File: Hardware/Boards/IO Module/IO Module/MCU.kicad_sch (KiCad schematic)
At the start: 21 parts, among them SW1 RST, U14 W25Q16JVUXIQ TR, U15 RP2040, Y3 12Mhz

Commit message: Completed IO Module PCB Layout
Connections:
- net MBUS_D0: now also U15.18 (GPIO15); no longer U15.11 (GPIO8)
- net MBUS_D1: now also U15.17 (GPIO14); no longer U15.12 (GPIO9)
- net MBUS_D10: now also U15.31 (GPIO20); no longer U15.29 (GPIO18)
- net MBUS_D11: now also U15.32 (GPIO21); no longer U15.30 (GPIO19)
- net MBUS_D12: now also U15.34 (GPIO22); no longer U15.31 (GPIO20)
- net MBUS_D13: now also U15.35 (GPIO23); no longer U15.32 (GPIO21)
- net MBUS_D14: now also U15.28 (GPIO17); no longer U15.34 (GPIO22)
- net MBUS_D15: now also U15.27 (GPIO16); no longer U15.35 (GPIO23)
- net MBUS_D2: now also U15.16 (GPIO13); no longer U15.13 (GPIO10)
- net MBUS_D3: now also U15.15 (GPIO12); no longer U15.14 (GPIO11)
- net MBUS_D4: now also U15.11 (GPIO8); no longer U15.15 (GPIO12)
- net MBUS_D5: now also U15.12 (GPIO9); no longer U15.16 (GPIO13)
- net MBUS_D6: now also U15.13 (GPIO10); no longer U15.17 (GPIO14)
- net MBUS_D7: now also U15.14 (GPIO11); no longer U15.18 (GPIO15)
- net MBUS_D8: now also U15.29 (GPIO18); no longer U15.27 (GPIO16)
- net MBUS_D9: now also U15.30 (GPIO19); no longer U15.28 (GPIO17)
- net USBPD_FLT_IN: now also U15.38 (GPIO26_ADC0); no longer U15.36 (GPIO24)
- net USBPD_SINK_EN: now also U15.36 (GPIO24); no longer U15.38 (GPIO26_ADC0)
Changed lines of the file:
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@@
+		)
+	)
+	(label "MBUS_D15"
+		(at 227.33 154.94 0)
+		(fields_autoplaced yes)
+		(effects
+			(font
+				(size 1.27 1.27)
+			)
+			(justify left bottom)
+		)
+	)
+	(label "MBUS_D6"
+		(at 227.33 139.7 0)
+		(fields_autoplaced yes)
+		(effects
+			(font
+				(size 1.27 1.27)
+			)
+			(justify left bottom)
 		)
 	)
@@
 		)
 	)
-	(label "MBUS_D0"
-		(at 227.33 134.62 0)
-		(fields_autoplaced yes)
-		(effects
-			(font
-				(size 1.27 1.27)
-			)
-			(justify left bottom)
-		)
-	)
 	(label "USBPD_PLG_EVNT"
 		(at 224.79 116.84 0)
@@
 		)
 	)
-	(label "MBUS_D13"
-		(at 227.33 167.64 0)
-		(fields_autoplaced yes)
-		(effects
-			(font
-				(size 1.27 1.27)
-			)
-			(justify left bottom)
-		)
-	)
-	(label "MBUS_D10"
-		(at 227.33 160.02 0)
-		(fields_autoplaced yes)
-		(effects
-			(font
-				(size 1.27 1.27)
-			)
-			(justify left bottom)
-		)
-	)
-	(label "MBUS_D15"
-		(at 227.33 172.72 0)
+	(label "MBUS_D7"
+		(at 227.33 142.24 0)
+		(fields_autoplaced yes)
+		(effects
+			(font
+				(size 1.27 1.27)
+			)
+			(justify left bottom)
+		)
+	)
+	(label "MBUS_D2"
+		(at 227.33 147.32 0)
 		(fields_autoplaced yes)
 		(effects
@@
 	)
 	(label "USBPD_FLT_IN"
-		(at 224.79 175.26 0)
-		(fields_autoplaced yes)
-		(effects
-			(font
-				(size 1.27 1.27)
-			)
-			(justify left bottom)
-		)
-	)
-	(label "MBUS_D14"
-		(at 227.33 170.18 0)
+		(at 224.79 182.88 0)
 		(fields_autoplaced yes)
 		(effects
@@
 		)
 	)
+	(label "MBUS_D12"
+		(at 227.33 170.18 0)
+		(fields_autoplaced yes)
+		(effects
+			(font
+				(size 1.27 1.27)
+			)
+			(justify left bottom)
+		)
+	)
 	(label "QSPI_D0"
 		(at 149.86 137.16 0)
@@
 		)
 	)
+	(label "MBUS_D3"
+		(at 227.33 144.78 0)
+		(fields_autoplaced yes)
+		(effects
+			(font
+				(size 1.27 1.27)
+			)
+			(justify left bottom)
+		)
+	)
 	(label "USBPD_CAP_MIS"
 		(at 224.79 187.96 0)
@@
 	)
 	(label "MBUS_D9"
-		(at 227.33 157.48 0)
-		(fields_autoplaced yes)
-		(effects
-			(font
-				(size 1.27 1.27)
-			)
-			(justify left bottom)
-		)
-	)
-	(label "MBUS_D7"
-		(at 227.33 152.4 0)
-		(fields_autoplaced yes)
-		(effects
-			(font
-				(size 1.27 1.27)
-			)
-			(justify left bottom)
-		)
-	)
-	(label "MBUS_D11"
 		(at 227.33 162.56 0)
 		(fields_autoplaced yes)
@@
 		)
 	)
-	(label "MBUS_D5"
-		(at 227.33 147.32 0)
-		(fields_autoplaced yes)
-		(effects
-			(font
-				(size 1.27 1.27)
-			)
-			(justify left bottom)
-		)
-	)
 	(label "MBUS_D[0..15]"
 		(at 262.89 132.08 0)
@@
 		)
 	)
-	(label "MBUS_D4"
-		(at 227.33 144.78 0)
-		(fields_autoplaced yes)
-		(effects
-			(font
-				(size 1.27 1.27)
-			)
-			(justify left bottom)
-		)
-	)
-	(label "MBUS_D2"
-		(at 227.33 139.7 0)
+	(label "MBUS_D5"
+		(at 227.33 137.16 0)
 		(fields_autoplaced yes)
 		(effects
@@
 		)
 	)
-	(label "MBUS_D3"
-		(at 227.33 142.24 0)
-		(fields_autoplaced yes)
-		(effects
-			(font
-				(size 1.27 1.27)
-			)
-			(justify left bottom)
-		)
-	)
-	(label "MBUS_D12"
-		(at 227.33 165.1 0)
+	(label "MBUS_D11"
+		(at 227.33 167.64 0)
 		(fields_autoplaced yes)
 		(effects
@@
 		)
 	)
-	(label "MBUS_D8"
-		(at 227.33 154.94 0)
+	(label "USBPD_SINK_EN"
+		(at 224.79 175.26 0)
 		(fields_autoplaced yes)
 		(effects
@@
 		)
 	)
-	(label "MBUS_D1"
-		(at 227.33 137.16 0)
-		(fields_autoplaced yes)
-		(effects
-			(font
-				(size 1.27 1.27)
-			)
-			(justify left bottom)
-		)
-	)
 	(label "GND"
 		(at 111.76 147.32 0)
@@
 		)
 	)
+	(label "MBUS_D8"
+		(at 227.33 160.02 0)
+		(fields_autoplaced yes)
+		(effects
+			(font
+				(size 1.27 1.27)
+			)
+			(justify left bottom)
+		)
+	)
 	(label "MCU_HB_LED"
 		(at 227.33 177.8 0)
@@
 		)
 	)
-	(label "USBPD_SINK_EN"
-		(at 224.79 182.88 0)
-		(fields_autoplaced yes)
-		(effects
-			(font
-				(size 1.27 1.27)
-			)
-			(justify left bottom)
-		)
-	)
-	(label "MBUS_D6"
-		(at 227.33 149.86 0)
+	(label "MBUS_D0"
+		(at 227.33 152.4 0)
 		(fields_autoplaced yes)
 		(effects
@@
 		)
 	)
+	(label "MBUS_D4"
+		(at 227.33 134.62 0)
+		(fields_autoplaced yes)
+		(effects
+			(font
+				(size 1.27 1.27)
+			)
+			(justify left bottom)
+		)
+	)
 	(label "VMCU_1V1"
 		(at 160.02 78.74 0)
@@
 		)
 	)
+	(label "MBUS_D10"
+		(at 227.33 165.1 0)
+		(fields_autoplaced yes)
+		(effects
+			(font
+				(size 1.27 1.27)
+			)
+			(justify left bottom)
+		)
+	)
+	(label "MBUS_D13"
+		(at 227.33 172.72 0)
+		(fields_autoplaced yes)
+		(effects
+			(font
+				(size 1.27 1.27)
+			)
+			(justify left bottom)
+		)
+	)
+	(label "MBUS_D1"
+		(at 227.33 149.86 0)
+		(fields_autoplaced yes)
+		(effects
+			(font
+				(size 1.27 1.27)
+			)
+			(justify left bottom)
+		)
+	)
 	(label "CAM_PWR_EN"
 		(at 241.3 119.38 180)
@@
 		)
 	)
+	(label "MBUS_D14"
+		(at 227.33 157.48 0)
+		(fields_autoplaced yes)
+		(effects
+			(font
+				(size 1.27 1.27)
+			)
+			(justify left bottom)
+		)
+	)
 	(hierarchical_label "CAM_PWR_EN"
 		(shape input)
@@
 		)
 	)
+	(hierarchical_label "CAM_LED_EN"
+		(shape input)
+		(at 241.3 121.92 0)
+		(fields_autoplaced yes)
+		(effects
+			(font
+				(size 1.27 1.27)
+			)
+			(justify left)
+		)
+	)
+	(hierarchical_label "MBUS_D[0..15]"
+		(shape input)
+		(at 281.94 132.08 0)
+		(fields_autoplaced yes)
+		(effects
+			(font
+				(size 1.27 1.27)
+			)
+			(justify left)
+		)
+	)
+	(hierarchical_label "USBPD_SINK_EN"
+		(shape input)
+		(at 241.3 175.26 0)
+		(fields_autoplaced yes)
+		(effects
+			(font
+				(size 1.27 1.27)
+			)
+			(justify left)
+		)
+	)
+	(hierarchical_label "I2C0_SCL"
+		(shape input)
+		(at 241.3 127 0)
+		(fields_autoplaced yes)
+		(effects
+			(font
+				(size 1.27 1.27)
+				(bold yes)
+			)
+			(justify left)
+		)
+	)
+	(hierarchical_label "I2C1_SCL"
+		(shape input)
+		(at 241.3 132.08 0)
+		(fields_autoplaced yes)
+		(effects
+			(font
+				(size 1.27 1.27)
+				(bold yes)
+			)
+			(justify left)
+		)
+	)
+	(hierarchical_label "USBPD_PLG_FLIP"
+		(shape input)
+		(at 241.3 114.3 0)
+		(fields_autoplaced yes)
+		(effects
+			(font
+				(size 1.27 1.27)
+			)
+			(justify left)
+		)
+	)
 	(hierarchical_label "USBPD_FLT_IN"
 		(shape input)
-		(at 241.3 175.26 0)
-		(fields_autoplaced yes)
-		(effects
-			(font
-				(size 1.27 1.27)
-			)
-			(justify left)
-		)
-	)
-	(hierarchical_label "CAM_LED_EN"
-		(shape input)
-		(at 241.3 121.92 0)
-		(fields_autoplaced yes)
-		(effects
-			(font
-				(size 1.27 1.27)
-			)
-			(justify left)
-		)
-	)
-	(hierarchical_label "MBUS_D[0..15]"
-		(shape input)
-		(at 281.94 132.08 0)
-		(fields_autoplaced yes)
-		(effects
-			(font
-				(size 1.27 1.27)
-			)
-			(justify left)
-		)
-	)
-	(hierarchical_label "I2C0_SCL"
-		(shape input)
-		(at 241.3 127 0)
-		(fields_autoplaced yes)
-		(effects
-			(font
-				(size 1.27 1.27)
-				(bold yes)
-			)
-			(justify left)
-		)
-	)
-	(hierarchical_label "I2C1_SCL"
-		(shape input)
-		(at 241.3 132.08 0)
-		(fields_autoplaced yes)
-		(effects
-			(font
-				(size 1.27 1.27)
-				(bold yes)
-			)
-			(justify left)
-		)
-	)
-	(hierarchical_label "USBPD_SINK_EN"
-		(shape input)
 		(at 241.3 182.88 0)
 		(fields_autoplaced yes)
 		(effects
-			(font
-				(size 1.27 1.27)
-			)
-			(justify left)
-		)
-	)
-	(hierarchical_label "USBPD_PLG_FLIP"
-		(shape input)
-		(at 241.3 114.3 0)
-		(fields_autoplaced yes)
-		(effects

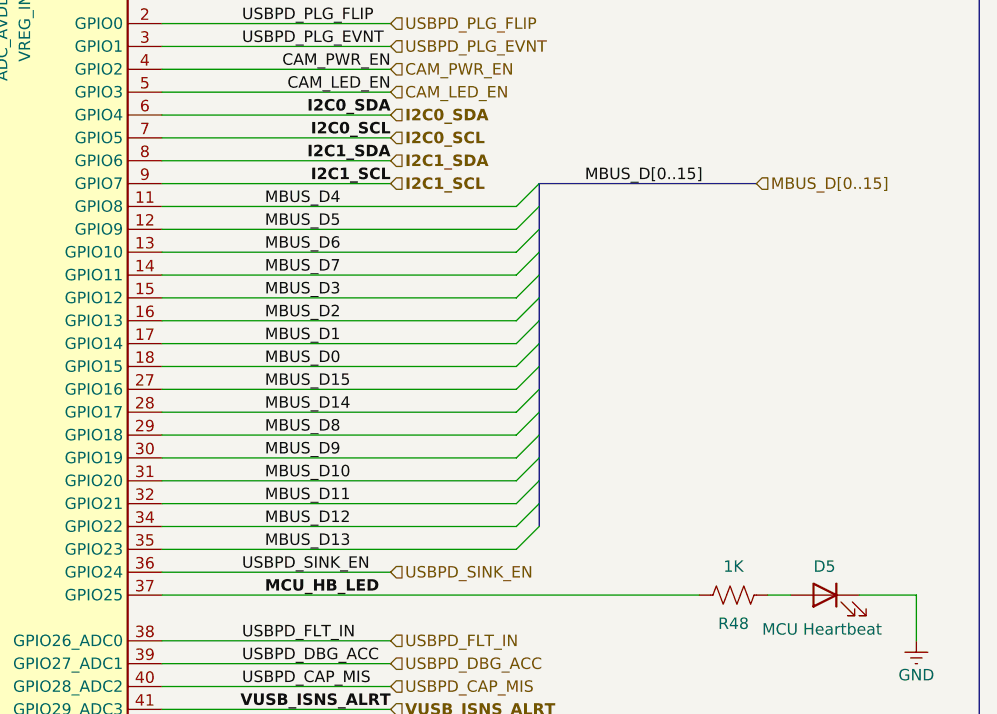
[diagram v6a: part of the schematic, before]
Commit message: Cleaned up routing for IO module
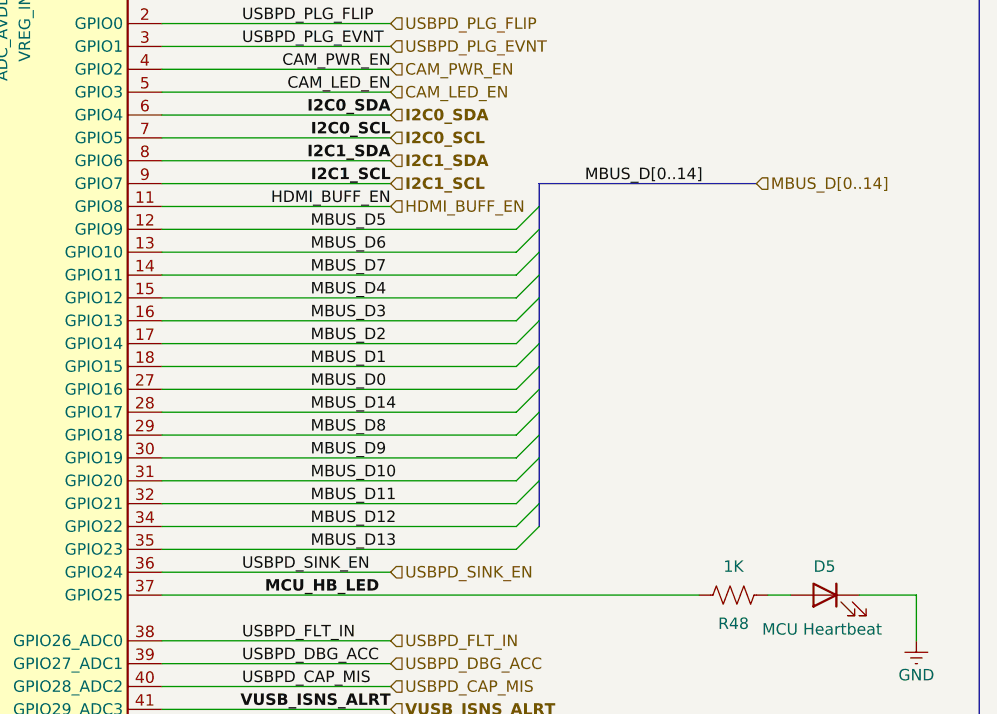
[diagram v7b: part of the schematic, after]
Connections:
- net MBUS_D15 is gone; now on net MBUS_D0: U15.27 (GPIO16)
- net MBUS_D0: no longer U15.18 (GPIO15)
- net MBUS_D1: now also U15.18 (GPIO15); no longer U15.17 (GPIO14)
- net MBUS_D2: now also U15.17 (GPIO14); no longer U15.16 (GPIO13)
- net MBUS_D3: now also U15.16 (GPIO13); no longer U15.15 (GPIO12)
- net MBUS_D4: now also U15.15 (GPIO12); no longer U15.11 (GPIO8)
- new net HDMI_BUFF_EN: U15.11 (GPIO8)
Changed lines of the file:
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@@
-	)
-	(bus_entry
-		(at 255.27 134.62)
-		(size 2.54 -2.54)
-		(stroke
-			(width 0)
-			(type default)
-		)
 	)
 	(bus_entry
@@
 	(wire
 		(pts
+			(xy 215.9 134.62) (xy 241.3 134.62)
+		)
+		(stroke
+			(width 0)
+			(type default)
+		)
+	)
+	(wire
+		(pts
 			(xy 215.9 147.32) (xy 255.27 147.32)
 		)
@@
 		(pts
 			(xy 215.9 172.72) (xy 255.27 172.72)
-		)
-		(stroke
-			(width 0)
-			(type default)
-		)
-	)
-	(wire
-		(pts
-			(xy 215.9 134.62) (xy 255.27 134.62)
 		)
 		(stroke
@@
 		)
 	)
-	(label "MBUS_D15"
-		(at 227.33 154.94 0)
-		(fields_autoplaced yes)
-		(effects
-			(font
-				(size 1.27 1.27)
-			)
-			(justify left bottom)
-		)
-	)
-	(label "MBUS_D6"
-		(at 227.33 139.7 0)
+	(label "MBUS_D9"
+		(at 232.41 162.56 0)
 		(fields_autoplaced yes)
 		(effects
@@
 		)
 	)
+	(label "MBUS_D5"
+		(at 232.41 137.16 0)
+		(fields_autoplaced yes)
+		(effects
+			(font
+				(size 1.27 1.27)
+			)
+			(justify left bottom)
+		)
+	)
+	(label "HDMI_BUFF_EN"
+		(at 241.3 134.62 180)
+		(fields_autoplaced yes)
+		(effects
+			(font
+				(size 1.27 1.27)
+			)
+			(justify right bottom)
+		)
+	)
 	(label "USBPD_PLG_EVNT"
 		(at 224.79 116.84 0)
@@
 		)
 	)
-	(label "MBUS_D7"
-		(at 227.33 142.24 0)
-		(fields_autoplaced yes)
-		(effects
-			(font
-				(size 1.27 1.27)
-			)
-			(justify left bottom)
-		)
-	)
-	(label "MBUS_D2"
-		(at 227.33 147.32 0)
-		(fields_autoplaced yes)
-		(effects
-			(font
-				(size 1.27 1.27)
-			)
-			(justify left bottom)
-		)
-	)
 	(label "USBPD_FLT_IN"
 		(at 224.79 182.88 0)
@@
 		)
 	)
-	(label "MBUS_D12"
-		(at 227.33 170.18 0)
-		(fields_autoplaced yes)
-		(effects
-			(font
-				(size 1.27 1.27)
-			)
-			(justify left bottom)
-		)
-	)
 	(label "QSPI_D0"
 		(at 149.86 137.16 0)
@@
 		)
 	)
-	(label "MBUS_D3"
-		(at 227.33 144.78 0)
+	(label "MBUS_D14"
+		(at 232.41 157.48 0)
 		(fields_autoplaced yes)
 		(effects
@@
 		)
 	)
-	(label "MBUS_D9"
-		(at 227.33 162.56 0)
+	(label "MBUS_D13"
+		(at 232.41 172.72 0)
 		(fields_autoplaced yes)
 		(effects
@@
 		)
 	)
-	(label "MBUS_D[0..15]"
+	(label "MBUS_D1"
+		(at 232.41 152.4 0)
+		(fields_autoplaced yes)
+		(effects
+			(font
+				(size 1.27 1.27)
+			)
+			(justify left bottom)
+		)
+	)
+	(label "MBUS_D[0..14]"
 		(at 262.89 132.08 0)
 		(fields_autoplaced yes)
@@
 		)
 	)
-	(label "MBUS_D5"
-		(at 227.33 137.16 0)
+	(label "MBUS_D4"
+		(at 232.41 144.78 0)
+		(fields_autoplaced yes)
+		(effects
+			(font
+				(size 1.27 1.27)
+			)
+			(justify left bottom)
+		)
+	)
+	(label "MBUS_D3"
+		(at 232.41 147.32 0)
+		(fields_autoplaced yes)
+		(effects
+			(font
+				(size 1.27 1.27)
+			)
+			(justify left bottom)
+		)
+	)
+	(label "MBUS_D0"
+		(at 232.41 154.94 0)
 		(fields_autoplaced yes)
 		(effects
@@
 		)
 	)
-	(label "MBUS_D11"
-		(at 227.33 167.64 0)
+	(label "MBUS_D12"
+		(at 232.41 170.18 0)
 		(fields_autoplaced yes)
 		(effects
@@
 		)
 	)
+	(label "MBUS_D2"
+		(at 232.41 149.86 0)
+		(fields_autoplaced yes)
+		(effects
+			(font
+				(size 1.27 1.27)
+			)
+			(justify left bottom)
+		)
+	)
 	(label "GND"
 		(at 111.76 147.32 0)
@@
 	)
 	(label "MBUS_D8"
-		(at 227.33 160.02 0)
+		(at 232.41 160.02 0)
 		(fields_autoplaced yes)
 		(effects
@@
 		)
 	)
-	(label "MBUS_D0"
-		(at 227.33 152.4 0)
+	(label "MBUS_D10"
+		(at 232.41 165.1 0)
+		(fields_autoplaced yes)
+		(effects
+			(font
+				(size 1.27 1.27)
+			)
+			(justify left bottom)
+		)
+	)
+	(label "MBUS_D7"
+		(at 232.41 142.24 0)
 		(fields_autoplaced yes)
 		(effects
@@
 		)
 	)
-	(label "MBUS_D4"
-		(at 227.33 134.62 0)
-		(fields_autoplaced yes)
-		(effects
-			(font
-				(size 1.27 1.27)
-			)
-			(justify left bottom)
-		)
-	)
 	(label "VMCU_1V1"
 		(at 160.02 78.74 0)
@@
 		)
 	)
+	(label "MBUS_D11"
+		(at 232.41 167.64 0)
+		(fields_autoplaced yes)
+		(effects
+			(font
+				(size 1.27 1.27)
+			)
+			(justify left bottom)
+		)
+	)
 	(label "QSPI_D2"
 		(at 149.86 142.24 0)
@@
 		)
 	)
-	(label "MBUS_D10"
-		(at 227.33 165.1 0)
-		(fields_autoplaced yes)
-		(effects
-			(font
-				(size 1.27 1.27)
-			)
-			(justify left bottom)
-		)
-	)
-	(label "MBUS_D13"
-		(at 227.33 172.72 0)
-		(fields_autoplaced yes)
-		(effects
-			(font
-				(size 1.27 1.27)
-			)
-			(justify left bottom)
-		)
-	)
-	(label "MBUS_D1"
-		(at 227.33 149.86 0)
+	(label "MBUS_D6"
+		(at 232.41 139.7 0)
 		(fields_autoplaced yes)
 		(effects
@@
 			)
 			(justify right bottom)
-		)
-	)
-	(label "MBUS_D14"
-		(at 227.33 157.48 0)
-		(fields_autoplaced yes)
-		(effects
-			(font
-				(size 1.27 1.27)
-			)
-			(justify left bottom)
 		)
 	)
@@
 		)
 	)
-	(hierarchical_label "MBUS_D[0..15]"
+	(hierarchical_label "MBUS_D[0..14]"
 		(shape input)
 		(at 281.94 132.08 0)
@@
 			)
 			(justify left)
+		)
+	)
+	(hierarchical_label "HDMI_BUFF_EN"
+		(shape input)
+		(at 241.3 134.62 0)
+		(fields_autoplaced yes)
+		(effects
+			(font
+				(size 1.27 1.27)
+			)
+			(justify left)
